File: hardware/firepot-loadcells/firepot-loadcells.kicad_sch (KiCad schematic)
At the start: 17 parts, among them U1 HX711, U2 HX711, U3 HX711, U4 HX711, U5 HX711, U6 HX711, U7 HX711, U8 HX711, U9 XIAO ESP32S3

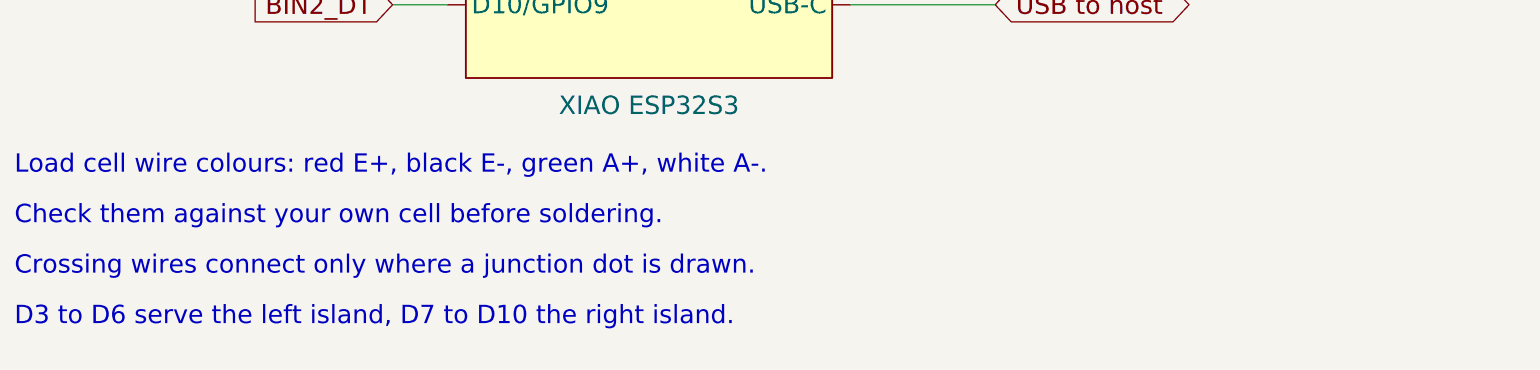
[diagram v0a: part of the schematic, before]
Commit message: Tier 2 rewritten as a build guide, with the real BOM
Replaces the first pass. Corrections from the developer's read, each
checked against source rather than the docs:

- Real parts throughout: CZL-611N 1kg cells, SmartElex HX711, WZATCO
  Yuva Go Plus, Lenovo 300 webcam, eSUN PLA. No soldering between
  boards: screw terminals and PCT-215 lever connectors.
- 3D printed parts committed to hardware/3d-printed/ and added to the
  steps. The plywood is 6mm and carries no weight; it stands on twelve
  printed pillars at the height of the bin tops, and the bins sit on
  printed bases on the table under it.
- The 440mm centre column is where the details, cart and checkout are
  drawn (UiLayer's 554px centre column), not a pot.
- Clone comes before the firmware flash; openFrameworks install added,
  including that the repo goes in apps/myApps (the vcxproj walks five
  levels up to OF_ROOT) and ofxFlowTools into addons.
- No Visual Studio version pinned. keystone.json dropped: the file is
  identity and keystone is done on the projector.
- Projector grid: 'Load measured layout' must run first, else there is
  nothing to nudge (index.html pgNudge).
- Explanation of behaviour cut throughout; that belongs to Tier 3.
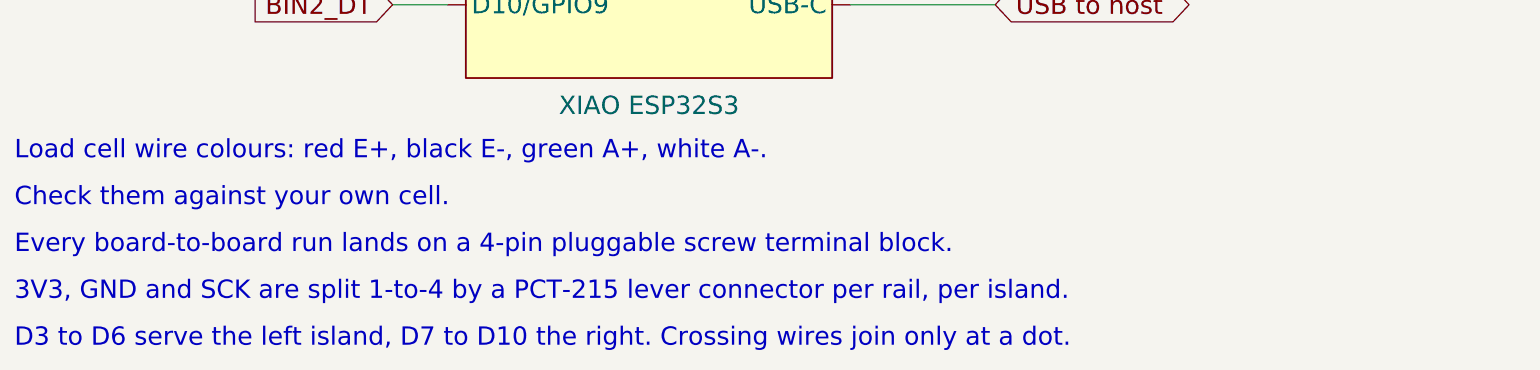
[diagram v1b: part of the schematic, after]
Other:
- note added: "3V3, GND and SCK are split 1-to-4 by a PCT-215 lever connector per rail, per island."
- note added: "Check them against your own cell."
- note added: "D3 to D6 serve the left island, D7 to D10 the right. Crossing wires join only at a dot."
- note added: "Every board-to-board run lands on a 4-pin pluggable screw terminal block."
- note removed: "Check them against your own cell before soldering."
- note removed: "Crossing wires connect only where a junction dot is drawn."
- note removed: "D3 to D6 serve the left island, D7 to D10 the right island."
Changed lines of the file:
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@@
 		(instances
 			(project "firepot-loadcells"
-				(path "/0acb1c25-fb10-4bdc-8da0-7b0f15f70c45"
+				(path "/b80b21b1-ad08-49e2-be60-56b782aa949f"
 					(reference "LC1") (unit 1)
 				)
@@
 		(instances
 			(project "firepot-loadcells"
-				(path "/0acb1c25-fb10-4bdc-8da0-7b0f15f70c45"
+				(path "/b80b21b1-ad08-49e2-be60-56b782aa949f"
 					(reference "U1") (unit 1)
 				)
@@
 		(instances
 			(project "firepot-loadcells"
-				(path "/0acb1c25-fb10-4bdc-8da0-7b0f15f70c45"
+				(path "/b80b21b1-ad08-49e2-be60-56b782aa949f"
 					(reference "LC2") (unit 1)
 				)
@@
 		(instances
 			(project "firepot-loadcells"
-				(path "/0acb1c25-fb10-4bdc-8da0-7b0f15f70c45"
+				(path "/b80b21b1-ad08-49e2-be60-56b782aa949f"
 					(reference "U2") (unit 1)
 				)
@@
 		(instances
 			(project "firepot-loadcells"
-				(path "/0acb1c25-fb10-4bdc-8da0-7b0f15f70c45"
+				(path "/b80b21b1-ad08-49e2-be60-56b782aa949f"
 					(reference "LC3") (unit 1)
 				)
@@
 		(instances
 			(project "firepot-loadcells"
-				(path "/0acb1c25-fb10-4bdc-8da0-7b0f15f70c45"
+				(path "/b80b21b1-ad08-49e2-be60-56b782aa949f"
 					(reference "U3") (unit 1)
 				)
@@
 		(instances
 			(project "firepot-loadcells"
-				(path "/0acb1c25-fb10-4bdc-8da0-7b0f15f70c45"
+				(path "/b80b21b1-ad08-49e2-be60-56b782aa949f"
 					(reference "LC4") (unit 1)
 				)
@@
 		(instances
 			(project "firepot-loadcells"
-				(path "/0acb1c25-fb10-4bdc-8da0-7b0f15f70c45"
+				(path "/b80b21b1-ad08-49e2-be60-56b782aa949f"
 					(reference "U4") (unit 1)
 				)
@@
 		(instances
 			(project "firepot-loadcells"
-				(path "/0acb1c25-fb10-4bdc-8da0-7b0f15f70c45"
+				(path "/b80b21b1-ad08-49e2-be60-56b782aa949f"
 					(reference "LC5") (unit 1)
 				)
@@
 		(instances
 			(project "firepot-loadcells"
-				(path "/0acb1c25-fb10-4bdc-8da0-7b0f15f70c45"
+				(path "/b80b21b1-ad08-49e2-be60-56b782aa949f"
 					(reference "U5") (unit 1)
 				)
@@
 		(instances
 			(project "firepot-loadcells"
-				(path "/0acb1c25-fb10-4bdc-8da0-7b0f15f70c45"
+				(path "/b80b21b1-ad08-49e2-be60-56b782aa949f"
 					(reference "LC6") (unit 1)
 				)
@@
 		(instances
 			(project "firepot-loadcells"
-				(path "/0acb1c25-fb10-4bdc-8da0-7b0f15f70c45"
+				(path "/b80b21b1-ad08-49e2-be60-56b782aa949f"
 					(reference "U6") (unit 1)
 				)
@@
 		(instances
 			(project "firepot-loadcells"
-				(path "/0acb1c25-fb10-4bdc-8da0-7b0f15f70c45"
+				(path "/b80b21b1-ad08-49e2-be60-56b782aa949f"
 					(reference "LC7") (unit 1)
 				)
@@
 		(instances
 			(project "firepot-loadcells"
-				(path "/0acb1c25-fb10-4bdc-8da0-7b0f15f70c45"
+				(path "/b80b21b1-ad08-49e2-be60-56b782aa949f"
 					(reference "U7") (unit 1)
 				)
@@
 		(instances
 			(project "firepot-loadcells"
-				(path "/0acb1c25-fb10-4bdc-8da0-7b0f15f70c45"
+				(path "/b80b21b1-ad08-49e2-be60-56b782aa949f"
 					(reference "LC8") (unit 1)
 				)
@@
 		(instances
 			(project "firepot-loadcells"
-				(path "/0acb1c25-fb10-4bdc-8da0-7b0f15f70c45"
+				(path "/b80b21b1-ad08-49e2-be60-56b782aa949f"
 					(reference "U8") (unit 1)
 				)
@@
 		(instances
 			(project "firepot-loadcells"
-				(path "/0acb1c25-fb10-4bdc-8da0-7b0f15f70c45"
+				(path "/b80b21b1-ad08-49e2-be60-56b782aa949f"
 					(reference "U9") (unit 1)
 				)
@@
 	(text "Load cell wire colours: red E+, black E-, green A+, white A-."
 		(exclude_from_sim no)
-		(at 12 430 0)
-		(effects (font (size 2.54 2.54)) (justify left))
-	)
-	(text "Check them against your own cell before soldering."
-		(exclude_from_sim no)
-		(at 12 437 0)
-		(effects (font (size 2.54 2.54)) (justify left))
-	)
-	(text "Crossing wires connect only where a junction dot is drawn."
-		(exclude_from_sim no)
-		(at 12 444 0)
-		(effects (font (size 2.54 2.54)) (justify left))
-	)
-	(text "D3 to D6 serve the left island, D7 to D10 the right island."
-		(exclude_from_sim no)
-		(at 12 451 0)
-		(effects (font (size 2.54 2.54)) (justify left))
-	)
+		(at 12 428 0)
+		(effects (font (size 2.54 2.54)) (justify left))
+	)
+	(text "Check them against your own cell."
+		(exclude_from_sim no)
+		(at 12 434.5 0)
+		(effects (font (size 2.54 2.54)) (justify left))
+	)
+	(text "Every board-to-board run lands on a 4-pin pluggable screw terminal block."
+		(exclude_from_sim no)
+		(at 12 441 0)
+		(effects (font (size 2.54 2.54)) (justify left))
+	)
+	(text "3V3, GND and SCK are split 1-to-4 by a PCT-215 lever connector per rail, per island."
+		(exclude_from_sim no)
+		(at 12 447.5 0)
+		(effects (font (size 2.54 2.54)) (justify left))
+	)
+	(text "D3 to D6 serve the left island, D7 to D10 the right. Crossing wires join only at a dot."
+		(exclude_from_sim no)
+		(at 12 454 0)
+		(effects (font (size 2.54 2.54)) (justify left))
+	)

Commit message: Tier 2: second round of corrections from the rig photos
- BOM: 2x M4 and 2x M5 bolts per cell, 12 screw terminal blocks, 6
  PCT-215 splitters (three per island, as the photo shows), white PLA
  for the corner plugs, and the table's own plywood top.
- The corner plugs round the plywood openings after the screen fabric
  is on, in white. The openings are cut with the corners taken off;
  plywood is not rounded. lotus_root dropped from the print list.
- Plywood order corrected: cut, cover, cut through, glue, then plugs.
- HX711 VCC and VDD shorted, both to 3V3. Schematic regenerated with a
  VDD pin so the sheet shows it.
- Projector and camera hang on one wall batten, projector at the
  ceiling and camera below it.
- Six photo slots placed inline through the build rather than at the end.
- Calibration is three bullets. Dropped the claim that the projector
  grid needs seeding first: it can start from zero. Rings are halos,
  and the wandering flame is idle behaviour only.
- Cut the LED heartbeat section and the 500 g prefill line.
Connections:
- net 3V3: now also U1.8 (VDD), U2.8 (VDD), U3.8 (VDD), U4.8 (VDD), U5.8 (VDD), U6.8 (VDD), U7.8 (VDD), U8.8 (VDD)
- net GND: now also U1.9 (GND), U2.9 (GND), U3.9 (GND), U4.9 (GND), U5.9 (GND), U6.9 (GND), U7.9 (GND), U8.9 (GND); no longer U1.8 (GND), U2.8 (GND), U3.8 (GND), U4.8 (GND), U5.8 (GND), U6.8 (GND), U7.8 (GND), U8.8 (GND)
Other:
- note added: "VCC and VDD are shorted at every HX711. Board-to-board runs use screw terminals."
- note removed: "Every board-to-board run lands on a 4-pin pluggable screw terminal block."
